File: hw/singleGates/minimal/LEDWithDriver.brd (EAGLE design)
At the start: 8 parts, among them Q1 BC817, Q2 BC817, Q3 BC817

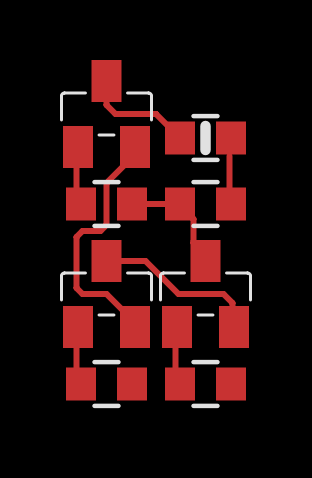
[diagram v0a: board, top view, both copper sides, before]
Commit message: Add led output and prepare first alu slice
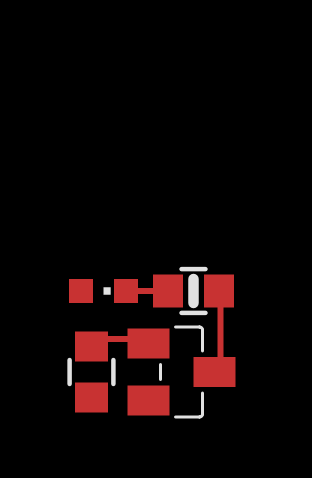
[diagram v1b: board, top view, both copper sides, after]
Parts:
- removed Q2, Q3: BC817, p.peter-gator:SOT23
- removed R3, R4: 10k, p.peter-gator:R0603
- removed R5: 1k, p.peter-rcl:R0603-MARK
- added L1: (no value), p.peter-leds:CHIPLED_0603
- R2: value 10k -> 1k; device p.peter-gator:R0603 -> p.peter-rcl:R0603-MARK
- moved R2 4.24 mm to (4.80, 4.50), turned to 0 degrees
- moved R1 3.82 mm to (1.40, 1.80), turned to 90 degrees
- moved Q1 2.72 mm to (4.40, 1.80), turned to 270 degrees
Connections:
- removed net AND: Q3.P$3, R5.1
- removed net B: R2.1
- removed net N$15: Q3.P$1, R4.1
- removed net N$2: Q1.P$3, R3.1, R4.2
- removed net N$3: Q2.P$1, R2.2
- removed net N$5: Q1.P$2, Q2.P$3
- new net INT: L1.C, R2.1
- new net N$1: Q1.P$3, R2.2
- net _VN: now also Q1.P$2; no longer Q2.P$2, Q3.P$2
- net _VP: now also L1.A; no longer R3.2, R5.2
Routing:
- net _VN: track 8.64 -> 0.28 mm
- net N$5: track 5.63 -> 0.00 mm
- net AND: track 4.20 -> 0.00 mm
- net N$2: track 3.95 -> 0.00 mm
- net N$1: track 0.00 -> 2.92 mm
- net N$15: track 2.07 -> 0.00 mm
- net N$3: track 2.07 -> 0.00 mm
- net _VP: track 1.74 -> 0.00 mm
- net INT: track 0.00 -> 1.40 mm
